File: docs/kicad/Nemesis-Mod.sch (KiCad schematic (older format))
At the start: 14 parts, among them M1-M2 Pololu G2 HighPower 18v18, M3 Pololu G2 HighPower 18v17, SW1 Rev SPDT Trigger, SW2 Firing SPDT Trigger, SW3 Reset SW Button

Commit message: Updating schematic.
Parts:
- added MCU1: Adafruit_Feather_M4_Express, symbol Nemesis-Mod:Adafruit_Feather_M4_Express
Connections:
- net 3V: now also MCU1.2 (3V); no longer MCU.~ (~RST)
- net 5V: now also MCU1.19 (USB); no longer MCU.~ (~RST)
- net FIRE_DOWN: now also MCU1.21 (12); no longer MCU.~ (~RST)
- net GNDREF: now also MCU1.4 (Gnd); no longer MCU.~ (~RST)
- net M1CS: now also MCU1.5 (A0); no longer MCU.~ (~RST)
- net M1PWM: now also MCU1.26 (5); no longer MCU.~ (~RST)
- net M1SLP: now also MCU1.24 (9); no longer MCU.~ (~RST)
- net M2CS: now also MCU1.6 (A1); no longer MCU.~ (~RST)
- net M2PWM: now also MCU1.25 (6); no longer MCU.~ (~RST)
- net M2SLP: now also MCU1.23 (10); no longer MCU.~ (~RST)
- net M3CS: now also MCU1.7 (A2); no longer MCU.~ (~RST)
- net M3PWM: now also MCU1.22 (11); no longer MCU.~ (~RST)
- net M3SLP: now also MCU1.8 (A3); no longer MCU.~ (~RST)
- net RESET_DOWN: now also MCU1.9 (A4); no longer MCU.~ (~RST)
- net REV_DOWN: now also MCU1.20 (13); no longer MCU.~ (~RST)
- net SCL: now also MCU1.27 (SCL); no longer MCU.~ (~RST)
- net SDA: now also MCU1.28 (SDA); no longer MCU.~ (~RST)
- net SOFT_LOCK1: now also MCU1.10 (A5); no longer MCU.~ (~RST)
- new net: BATT.1 (+), M1-M2.~ (VREG), M3.~ (~SLP)
- new net: BATT.2 (-), M1-M2.~ (VREG), M3.~ (~SLP)
- no-connect marks 31 -> 33
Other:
- moved on the sheet: MCU
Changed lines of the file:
@@
 L Nemesis-Mod:Adafruit_nRF52_Feather MCU
 U 1 1 5DBD8417
-P 2200 2200
-F 0 "MCU" H 2200 3615 50  0000 C CNN
-F 1 "Adafruit nRF52832 Feather" H 2200 3524 50  0000 C CNN
-F 2 "" H 2850 900 50  0001 C CNN
-F 3 "" H 2850 900 50  0001 C CNN
-	1    2200 2200
+P -900 2100
+F 0 "MCU" H -900 3515 50  0000 C CNN
+F 1 "Adafruit nRF52832 Feather" H -900 3424 50  0000 C CNN
+F 2 "" H -250 800 50  0001 C CNN
+F 3 "" H -250 800 50  0001 C CNN
+	1    -900 2100
 	1    0    0    -1
 $EndComp
@@
 RESET_DOWN
 $Comp
-L power:GNDREF #PWR?
+L power:GNDREF #PWR0101
 U 1 1 5F5EA087
 P 1050 1350
-F 0 "#PWR?" H 1050 1100 50  0001 C CNN
+F 0 "#PWR0101" H 1050 1100 50  0001 C CNN
 F 1 "GNDREF" H 1055 1177 50  0000 C CNN
 F 2 "" H 1050 1350 50  0001 C CNN
@@
 $EndComp
 $Comp
-L power:GNDREF #PWR?
+L power:GNDREF #PWR0102
 U 1 1 5F5EA7BC
 P 4950 950
-F 0 "#PWR?" H 4950 700 50  0001 C CNN
+F 0 "#PWR0102" H 4950 700 50  0001 C CNN
 F 1 "GNDREF" H 4955 777 50  0000 C CNN
 F 2 "" H 4950 950 50  0001 C CNN
@@
 	4950 1050 4950 950
 $Comp
-L power:GNDREF #PWR?
+L power:GNDREF #PWR0103
 U 1 1 5F5FC40A
 P 6100 5500
-F 0 "#PWR?" H 6100 5250 50  0001 C CNN
+F 0 "#PWR0103" H 6100 5250 50  0001 C CNN
 F 1 "GNDREF" H 6105 5327 50  0000 C CNN
 F 2 "" H 6100 5500 50  0001 C CNN
@@
 	6100 5200 6100 5500
 $Comp
-L power:GNDREF #PWR?
+L power:GNDREF #PWR0104
 U 1 1 5F600FD0
 P 3600 3950
-F 0 "#PWR?" H 3600 3700 50  0001 C CNN
+F 0 "#PWR0104" H 3600 3700 50  0001 C CNN
 F 1 "GNDREF" H 3605 3777 50  0000 C CNN
 F 2 "" H 3600 3950 50  0001 C CNN
@@
 	3600 4050 3600 3950
 $Comp
-L power:GNDREF #PWR?
+L power:GNDREF #PWR0105
 U 1 1 5F61012E
 P 4200 5950
-F 0 "#PWR?" H 4200 5700 50  0001 C CNN
+F 0 "#PWR0105" H 4200 5700 50  0001 C CNN
 F 1 "GNDREF" H 4205 5777 50  0000 C CNN
 F 2 "" H 4200 5950 50  0001 C CNN
@@
 $EndComp
 $Comp
-L power:GNDREF #PWR?
+L power:GNDREF #PWR0106
 U 1 1 5F610CDE
 P 2100 5150
-F 0 "#PWR?" H 2100 4900 50  0001 C CNN
+F 0 "#PWR0106" H 2100 4900 50  0001 C CNN
 F 1 "GNDREF" H 2105 4977 50  0000 C CNN
 F 2 "" H 2100 5150 50  0001 C CNN
@@
 $EndComp
 $Comp
-L power:GNDREF #PWR?
+L power:GNDREF #PWR0107
 U 1 1 5F610FC3
 P 2600 5950
-F 0 "#PWR?" H 2600 5700 50  0001 C CNN
+F 0 "#PWR0107" H 2600 5700 50  0001 C CNN
 F 1 "GNDREF" H 2605 5777 50  0000 C CNN
 F 2 "" H 2600 5950 50  0001 C CNN
@@
 $EndComp
 $Comp
-L power:GNDREF #PWR?
+L power:GNDREF #PWR0108
 U 1 1 5F6112BA
 P 2350 7050
-F 0 "#PWR?" H 2350 6800 50  0001 C CNN
+F 0 "#PWR0108" H 2350 6800 50  0001 C CNN
 F 1 "GNDREF" H 2355 6877 50  0000 C CNN
 F 2 "" H 2350 7050 50  0001 C CNN
@@
 Wire Wire Line
 	2100 4950 2100 5150
+$Comp
+L Nemesis-Mod:Adafruit_Feather_M4_Express MCU1
+U 1 1 619F6DFB
+P 2200 2200
+F 0 "MCU1" H 2200 3615 50  0000 C CNN
+F 1 "Adafruit_Feather_M4_Express" H 2200 3524 50  0000 C CNN
+F 2 "" H 2850 900 50  0001 C CNN
+F 3 "" H 2850 900 50  0001 C CNN
+	1    2200 2200
+	1    0    0    -1
+$EndComp
+NoConn ~ 2900 1050
+NoConn ~ 2900 1200
 $EndSCHEMATC

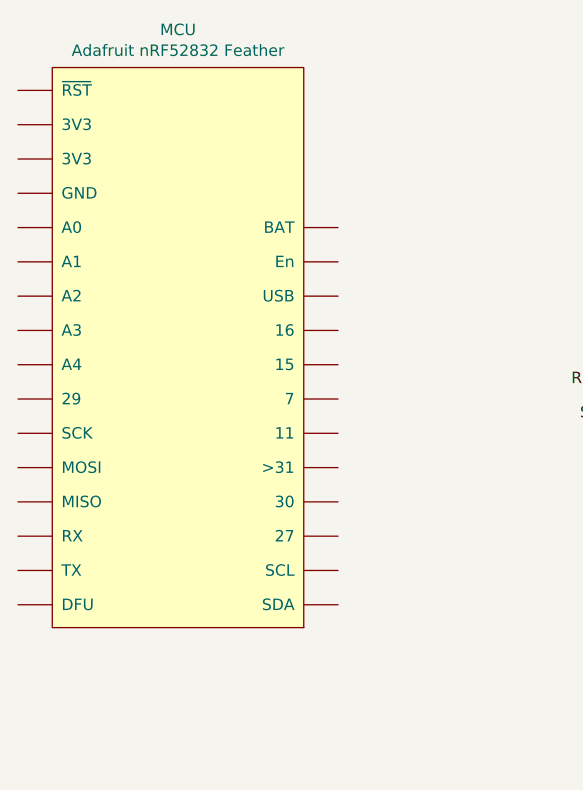
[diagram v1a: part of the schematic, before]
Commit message: Correcting MCU1 to Feather M4.
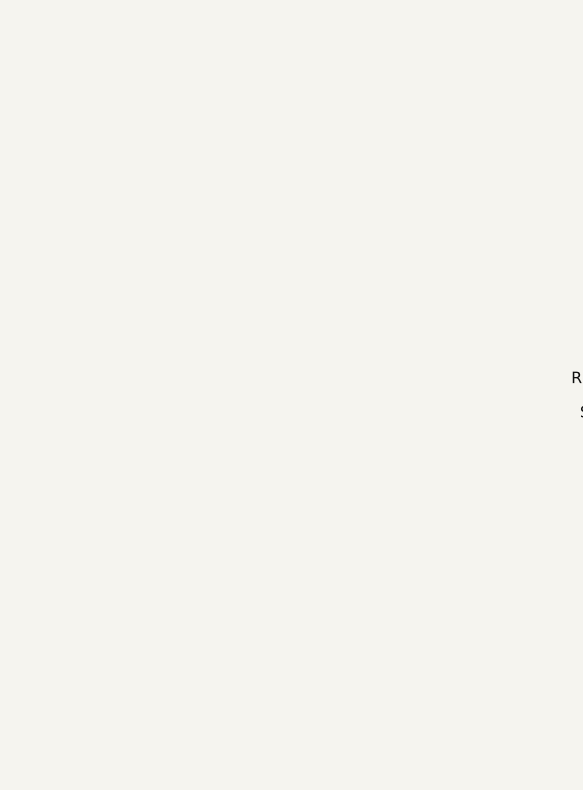
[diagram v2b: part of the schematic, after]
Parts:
- removed MCU: Adafruit nRF52832 Feather, symbol Nemesis-Mod:Adafruit_nRF52_Feather
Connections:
- new net: BATT.1 (+), M1-M2.~ (VREG), M3.~ (~SLP)
- new net: BATT.2 (-), M1-M2.~ (VREG), M3.~ (~SLP)
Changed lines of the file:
@@
 Text GLabel 2900 1950 2    50   Input ~ 0
 5V
-$Comp
-L Nemesis-Mod:Adafruit_nRF52_Feather MCU
-U 1 1 5DBD8417
-P -900 2100
-F 0 "MCU" H -900 3515 50  0000 C CNN
-F 1 "Adafruit nRF52832 Feather" H -900 3424 50  0000 C CNN
-F 2 "" H -250 800 50  0001 C CNN
-F 3 "" H -250 800 50  0001 C CNN
-	1    -900 2100
-	1    0    0    -1
-$EndComp
 NoConn ~ 2900 1650
 NoConn ~ 2900 1800

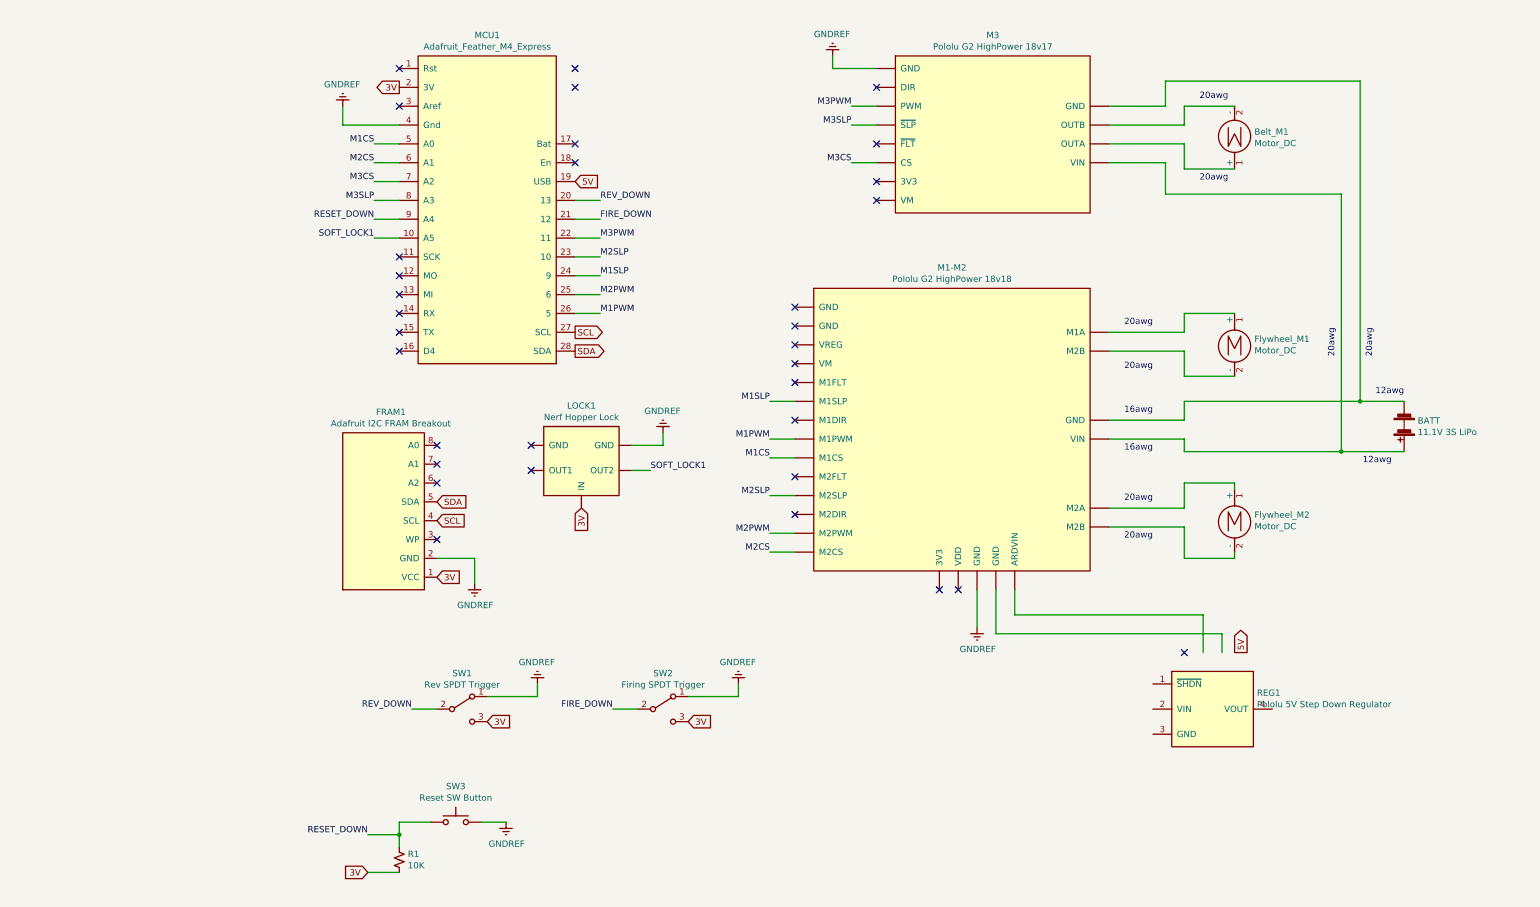
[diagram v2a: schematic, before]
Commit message: Adding custom board for consolidating pins.
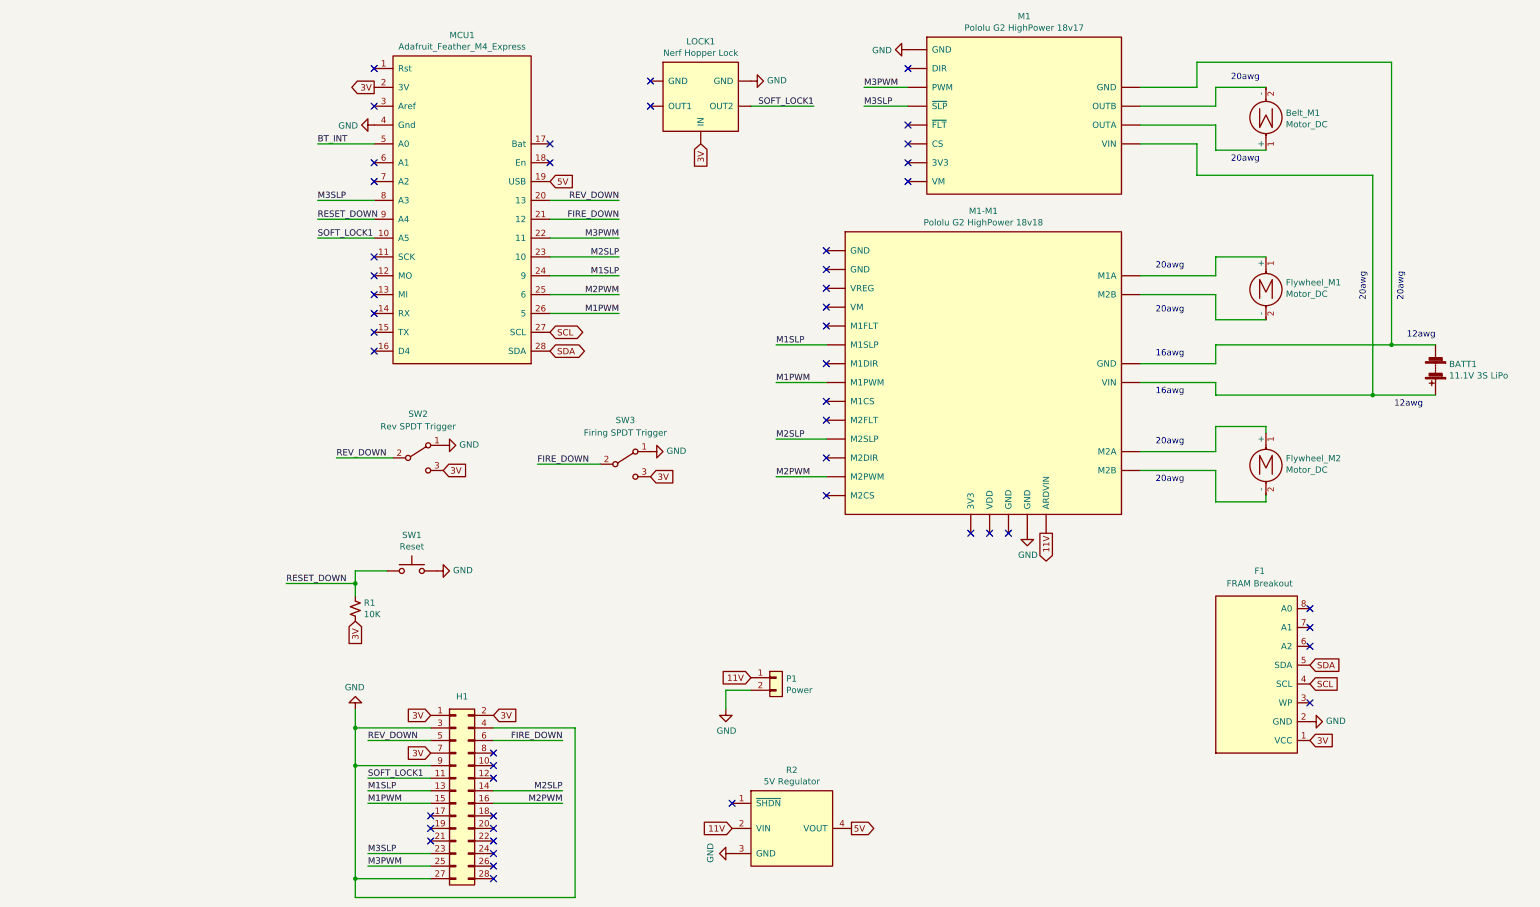
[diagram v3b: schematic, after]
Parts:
- removed FRAM1: Adafruit I2C FRAM Breakout, symbol Nemesis-Mod:Adafruit_I2C_FRAM_Breakout
- removed REG1: Pololu 5V Step Down Regulator, symbol Nemesis-Mod:Pololu_5V_Step_Down_Regulator
- added F1: FRAM Breakout, Connector_PinHeader_2.54mm:PinHeader_1x08_P2.54mm_Vertical, symbol Nemesis-Mod:Adafruit_I2C_FRAM_Breakout
- added H1: (no value), Connector_PinHeader_2.54mm:PinHeader_2x14_P2.54mm_Vertical, symbol Connector_Generic:Conn_02x14_Odd_Even
- added P1: Power, Connector_PinHeader_2.54mm:PinHeader_1x02_P2.54mm_Vertical, symbol Connector_Generic:Conn_01x02
- added R2: 5V Regulator, Connector_PinHeader_2.54mm:PinHeader_1x04_P2.54mm_Vertical, symbol Nemesis-Mod:Pololu_5V_Step_Down_Regulator
- MCU1: footprint (none) -> Adafruit:Adafruit_Feather_M4_Express
- R1: footprint (none) -> Resistor_THT:R_Axial_DIN0207_L6.3mm_D2.5mm_P5.08mm_Vertical
- SW1: renamed from SW3; value Reset SW Button -> Reset; footprint (none) -> Button_Switch_THT:SW_PUSH_6mm; MPID (none) -> 367 (Adafruit)
- renumbered BATT to BATT1, M3 to M1, M1-M2 to M1-M1, SW1 to SW2, SW2 to SW3
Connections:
- net 3V: now also F1.1 (VCC), H1.1 (Pin_1), H1.2 (Pin_2), H1.7 (Pin_7)
- net 5V: now also R2.4 (VOUT)
- net FIRE_DOWN: now also H1.6 (Pin_6)
- net M1PWM: now also H1.15 (Pin_15)
- net M1SLP: now also H1.13 (Pin_13)
- net M2PWM: now also H1.16 (Pin_16)
- net M2SLP: now also H1.14 (Pin_14)
- net M3PWM: now also H1.25 (Pin_25)
- net M3SLP: now also H1.23 (Pin_23)
- net REV_DOWN: now also H1.5 (Pin_5)
- net SCL: now also F1.4 (SCL)
- net SDA: now also F1.5 (SDA)
- net SOFT_LOCK1: now also H1.11 (Pin_11)
- net GNDREF renamed GND
- net GND: now also F1.2 (GND), H1.27 (Pin_27), H1.3 (Pin_3), H1.4 (Pin_4), H1.9 (Pin_9), P1.2 (Pin_2), R2.3 (GND)
- net M1CS renamed BT_INT
- net BT_INT: no longer M1-M1.~ (VREG)
- net M2CS: no longer names the net of MCU1.6 (A1)
- net M2CS: no longer M1-M1.~ (VREG)
- net M3CS: no longer names the net of MCU1.7 (A2)
- net M3CS: no longer M1.~ (~SLP)
- new net: BATT1.1 (+), M1-M1.~ (VREG), M1.~ (~SLP)
- new net: BATT1.2 (-), M1-M1.~ (VREG), M1.~ (~SLP)
- new net 11V: M1-M1.~ (VREG), P1.1 (Pin_1), R2.2 (VIN)
- no-connect marks 33 -> 49
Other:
- moved on the sheet: BATT1, Belt_M1, Flywheel_M1, Flywheel_M2, LOCK1, M1, M1-M1, R1, SW1, SW2, SW3
